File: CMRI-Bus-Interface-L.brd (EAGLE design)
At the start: 66 x 100 mm, 20 parts, among them CON1 0.100, CON2 0.100, U1 MAX3465CPD

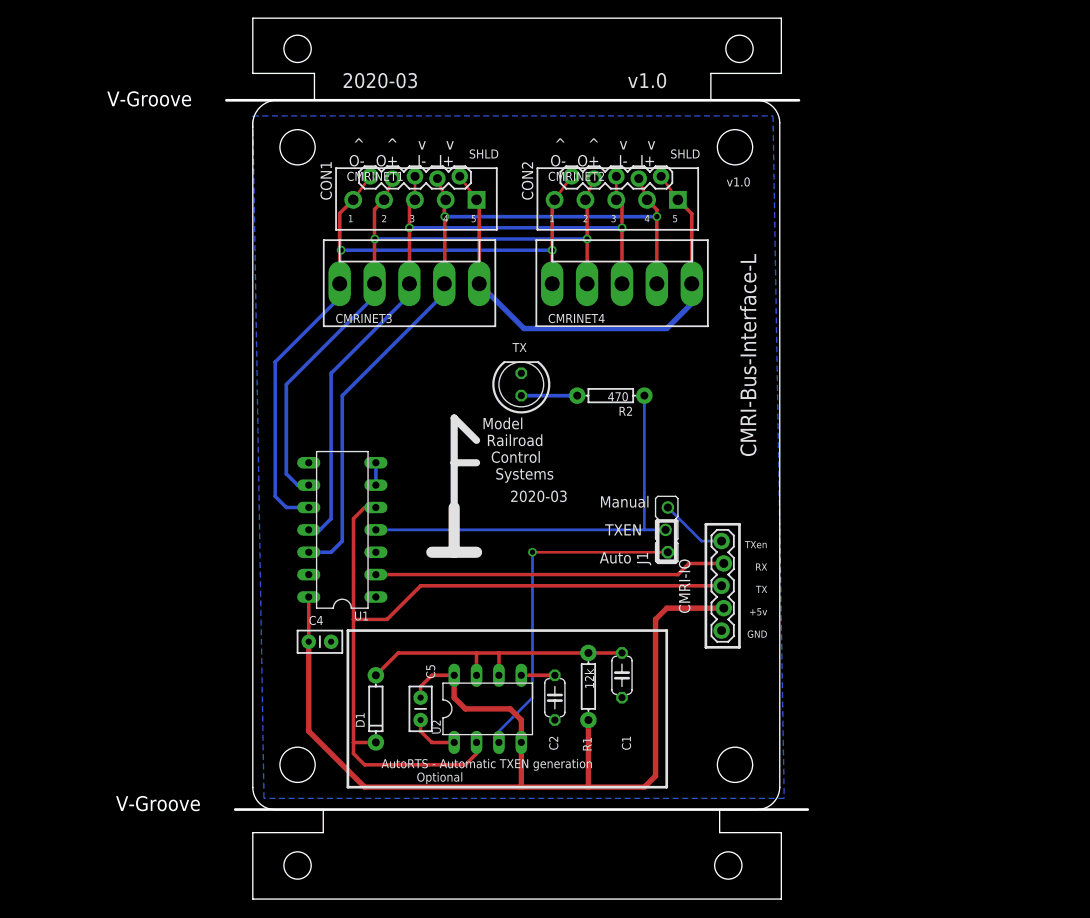
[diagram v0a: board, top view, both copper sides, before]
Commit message: v1.1 - changed BOARD to be a 10cmx10cm size so that V-Scores allowed
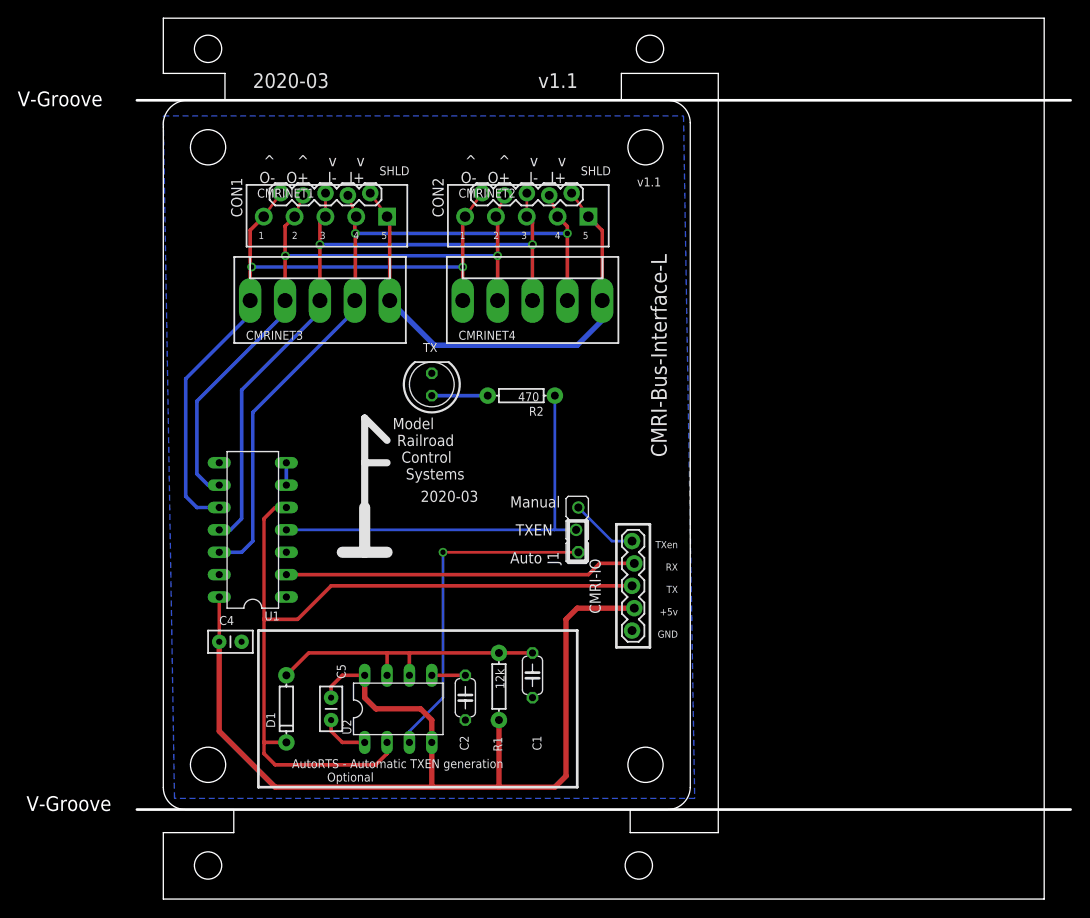
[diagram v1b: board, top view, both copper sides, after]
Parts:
- moved CMRINET4 10.3 mm to (41.9, 67.9)
- moved CMRINET1 10.3 mm to (17.8, 77.5)
- moved CMRINET3 10.3 mm to (17.8, 67.9)
- moved CON1 10.3 mm to (13.3, 80.0)
- moved CMRINET2 10.3 mm to (40.6, 77.5)
- moved CON2 10.3 mm to (36.2, 80.0)
- moved C1 10.2 mm to (41.9, 25.4)
- moved C2 10.2 mm to (34.3, 22.9)
- moved U$3 10.2 mm to (22.9, 39.4)
- moved BOARD1 10.2 mm to (0.00, 0.00)
- moved C4 10.2 mm to (7.62, 29.2)
- moved C5 10.2 mm to (19.1, 21.6)
- moved TX 10.2 mm to (30.5, 58.4)
- moved U1 10.2 mm to (10.2, 41.9)
- moved D1 10.2 mm to (14.0, 21.6)
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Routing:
- net OUT-: track 82.1 -> 80.2 mm
- net IN+: track 87.2 -> 85.3 mm
- net OUT+: track 77.9 -> 75.9 mm
- net IN-: track 82.5 -> 80.6 mm
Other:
- board size 66 x 100 mm -> 106 x 100 mm
- board text added: "v1.1"
- board text removed: "v1.0"

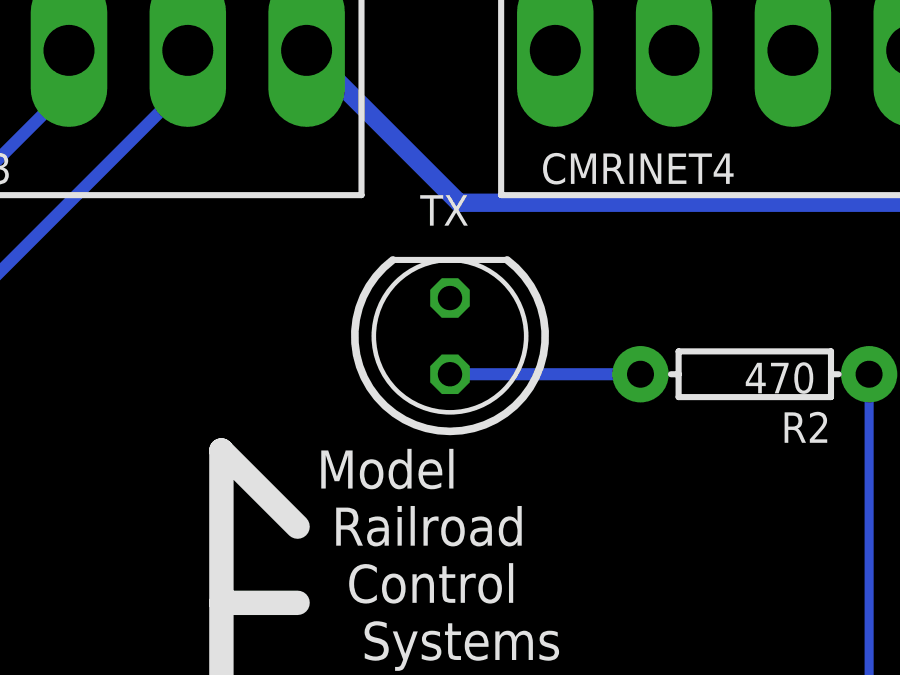
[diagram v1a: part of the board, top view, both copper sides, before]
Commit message: added missing component values
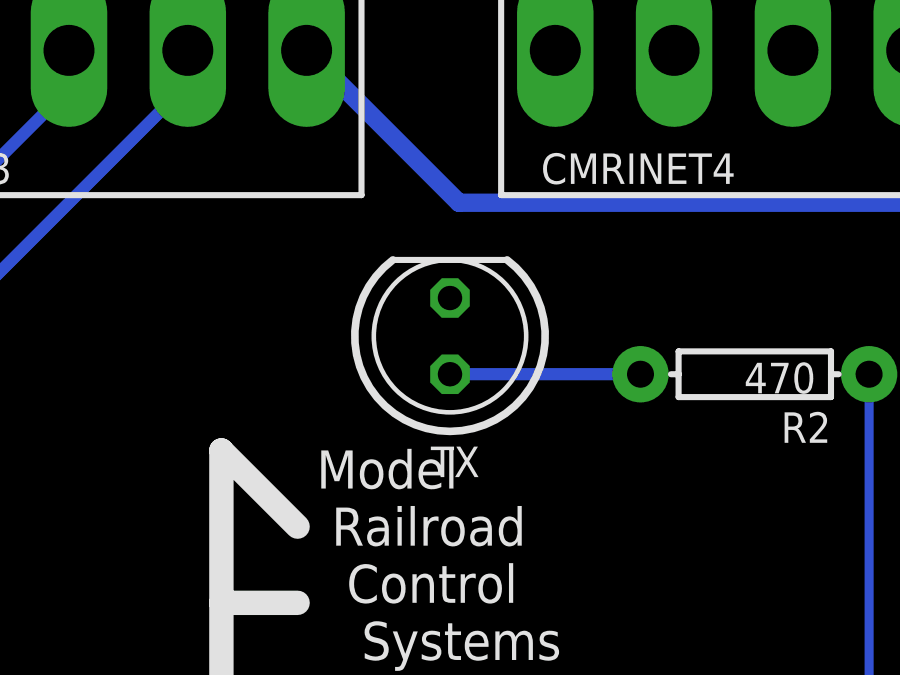
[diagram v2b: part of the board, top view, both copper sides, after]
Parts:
- CMRI-IO: value (none) -> 0.100; device SPCoast:CON-CMRI-IO -> SPCoast:1X05-CMRI-IO
- CMRINET3, CMRINET4: value Molex -> 0.156
- U2: value (none) -> NE555
- turned TX to 270 degrees
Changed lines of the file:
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@@
 <layer number="20" name="Dimension" color="15" fill="1" visible="yes" active="yes"/>
 <layer number="21" name="tPlace" color="19" fill="1" visible="yes" active="yes"/>
-<layer number="22" name="bPlace" color="17" fill="1" visible="yes" active="yes"/>
+<layer number="22" name="bPlace" color="17" fill="1" visible="no" active="yes"/>
 <layer number="23" name="tOrigins" color="30" fill="1" visible="yes" active="yes"/>
-<layer number="24" name="bOrigins" color="15" fill="1" visible="yes" active="yes"/>
+<layer number="24" name="bOrigins" color="15" fill="1" visible="no" active="yes"/>
 <layer number="25" name="tNames" color="63" fill="1" visible="yes" active="yes"/>
-<layer number="26" name="bNames" color="34" fill="1" visible="yes" active="yes"/>
+<layer number="26" name="bNames" color="34" fill="1" visible="no" active="yes"/>
 <layer number="27" name="tValues" color="56" fill="1" visible="yes" active="yes"/>
-<layer number="28" name="bValues" color="7" fill="1" visible="yes" active="yes"/>
-<layer number="29" name="tStop" color="7" fill="3" visible="yes" active="yes"/>
-<layer number="30" name="bStop" color="7" fill="6" visible="yes" active="yes"/>
-<layer number="31" name="tCream" color="7" fill="4" visible="yes" active="yes"/>
-<layer number="32" name="bCream" color="7" fill="5" visible="yes" active="yes"/>
-<layer number="33" name="tFinish" color="6" fill="3" visible="yes" active="yes"/>
-<layer number="34" name="bFinish" color="6" fill="6" visible="yes" active="yes"/>
-<layer number="35" name="tGlue" color="7" fill="4" visible="yes" active="yes"/>
-<layer number="36" name="bGlue" color="7" fill="5" visible="yes" active="yes"/>
-<layer number="37" name="tTest" color="7" fill="1" visible="yes" active="yes"/>
-<layer number="38" name="bTest" color="7" fill="1" visible="yes" active="yes"/>
-<layer number="39" name="tKeepout" color="4" fill="11" visible="yes" active="yes"/>
-<layer number="40" name="bKeepout" color="3" fill="11" visible="yes" active="yes"/>
-<layer number="41" name="tRestrict" color="4" fill="10" visible="yes" active="yes"/>
-<layer number="42" name="bRestrict" color="3" fill="10" visible="yes" active="yes"/>
-<layer number="43" name="vRestrict" color="2" fill="10" visible="yes" active="yes"/>
+<layer number="28" name="bValues" color="7" fill="1" visible="no" active="yes"/>
+<layer number="29" name="tStop" color="7" fill="3" visible="no" active="yes"/>
+<layer number="30" name="bStop" color="7" fill="6" visible="no" active="yes"/>
+<layer number="31" name="tCream" color="7" fill="4" visible="no" active="yes"/>
+<layer number="32" name="bCream" color="7" fill="5" visible="no" active="yes"/>
+<layer number="33" name="tFinish" color="6" fill="3" visible="no" active="yes"/>
+<layer number="34" name="bFinish" color="6" fill="6" visible="no" active="yes"/>
+<layer number="35" name="tGlue" color="7" fill="4" visible="no" active="yes"/>
+<layer number="36" name="bGlue" color="7" fill="5" visible="no" active="yes"/>
+<layer number="37" name="tTest" color="7" fill="1" visible="no" active="yes"/>
+<layer number="38" name="bTest" color="7" fill="1" visible="no" active="yes"/>
+<layer number="39" name="tKeepout" color="4" fill="11" visible="no" active="yes"/>
+<layer number="40" name="bKeepout" color="3" fill="11" visible="no" active="yes"/>
+<layer number="41" name="tRestrict" color="4" fill="10" visible="no" active="yes"/>
+<layer number="42" name="bRestrict" color="3" fill="10" visible="no" active="yes"/>
+<layer number="43" name="vRestrict" color="2" fill="10" visible="no" active="yes"/>
 <layer number="44" name="Drills" color="16" fill="1" visible="yes" active="yes"/>
 <layer number="45" name="Holes" color="35" fill="1" visible="yes" active="yes"/>
@@
 <layer number="48" name="Document" color="47" fill="1" visible="yes" active="yes"/>
 <layer number="49" name="Reference" color="48" fill="1" visible="yes" active="yes"/>
-<layer number="50" name="dxf" color="7" fill="1" visible="yes" active="yes"/>
+<layer number="50" name="dxf" color="7" fill="1" visible="no" active="yes"/>
 <layer number="51" name="tDocu" color="24" fill="1" visible="yes" active="yes"/>
-<layer number="52" name="bDocu" color="7" fill="1" visible="yes" active="yes"/>
+<layer number="52" name="bDocu" color="7" fill="1" visible="no" active="yes"/>
 <layer number="91" name="Nets" color="2" fill="1" visible="no" active="no"/>
 <layer number="92" name="Busses" color="1" fill="1" visible="no" active="no"/>
@@
 <attribute name="VALUE" x="42.672" y="57.531" size="1.016" layer="21" font="vector" ratio="15" rot="R180"/>
 </element>
-<element name="CMRINET3" library="SPCoast" package="KK-156-5" value="Molex" x="17.78" y="67.945" smashed="yes">
+<element name="CMRINET3" library="SPCoast" package="KK-156-5" value="0.156" x="17.78" y="67.945" smashed="yes">
 <attribute name="NAME" x="15.875" y="64.51" size="1.016" layer="25" font="vector" ratio="10" rot="R180"/>
 <attribute name="VALUE" x="25.4" y="65.03" size="1.016" layer="27" font="vector" ratio="10" rot="R180"/>
 </element>
-<element name="CMRINET4" library="SPCoast" package="KK-156-5" value="Molex" x="41.91" y="67.945" smashed="yes">
+<element name="CMRINET4" library="SPCoast" package="KK-156-5" value="0.156" x="41.91" y="67.945" smashed="yes">
 <attribute name="NAME" x="40.005" y="64.51" size="1.016" layer="25" font="vector" ratio="10" rot="R180"/>
 <attribute name="VALUE" x="50.165" y="65.03" size="1.016" layer="27" font="vector" ratio="10" rot="R180"/>
 </element>
-<element name="TX" library="SPCoast" package="LED5MM" value="" x="30.48" y="58.42" smashed="yes" rot="R90">
-<attribute name="NAME" x="31.115" y="63.119" size="1.016" layer="25" font="vector" ratio="10" rot="R180"/>
-<attribute name="VALUE" x="32.131" y="60.325" size="1.27" layer="27" ratio="10" rot="R90"/>
+<element name="TX" library="SPCoast" package="LED5MM" value="" x="30.48" y="58.42" smashed="yes" rot="R270">
+<attribute name="NAME" x="29.845" y="53.721" size="1.016" layer="25" font="vector" ratio="10"/>
+<attribute name="VALUE" x="28.829" y="56.515" size="1.27" layer="27" ratio="10" rot="R270"/>
 </element>
 <element name="U1" library="SPCoast" package="DIL14" value="MAX3465CPD" x="10.16" y="41.91" smashed="yes" rot="R90">
@@
 <attribute name="VALUE" x="10.795" y="35.179" size="1.016" layer="27" font="vector" ratio="10" rot="R90"/>
 </element>
-<element name="U2" library="SPCoast" package="DIL-08" value="" x="26.67" y="21.59" smashed="yes">
+<element name="U2" library="SPCoast" package="DIL-08" value="NE555" x="26.67" y="21.59" smashed="yes">
 <attribute name="MF" value="Arrow Electronics" x="26.67" y="21.59" size="1.778" layer="27" display="off"/>
 <attribute name="OC_NEWARK" value="89K1486" x="26.67" y="21.59" size="1.778" layer="27" display="off"/>
@@
 <attribute name="VALUE" x="31.75" y="76.2" size="1.016" layer="27" font="vector" ratio="10" rot="R180"/>
 </element>
-<element name="CMRI-IO" library="SPCoast" package="CON-CMRI-IO" value="" x="53.34" y="30.48" smashed="yes" rot="R90">
+<element name="CMRI-IO" library="SPCoast" package="1X05-CMRI-IO" value="0.100" x="53.34" y="30.48" smashed="yes" rot="R90">
 <attribute name="NAME" x="49.657" y="32.385" size="1.27" layer="25" font="vector" rot="R90"/>
 <attribute name="VALUE" x="56.642" y="29.21" size="1.27" layer="27" font="vector" rot="R90"/>

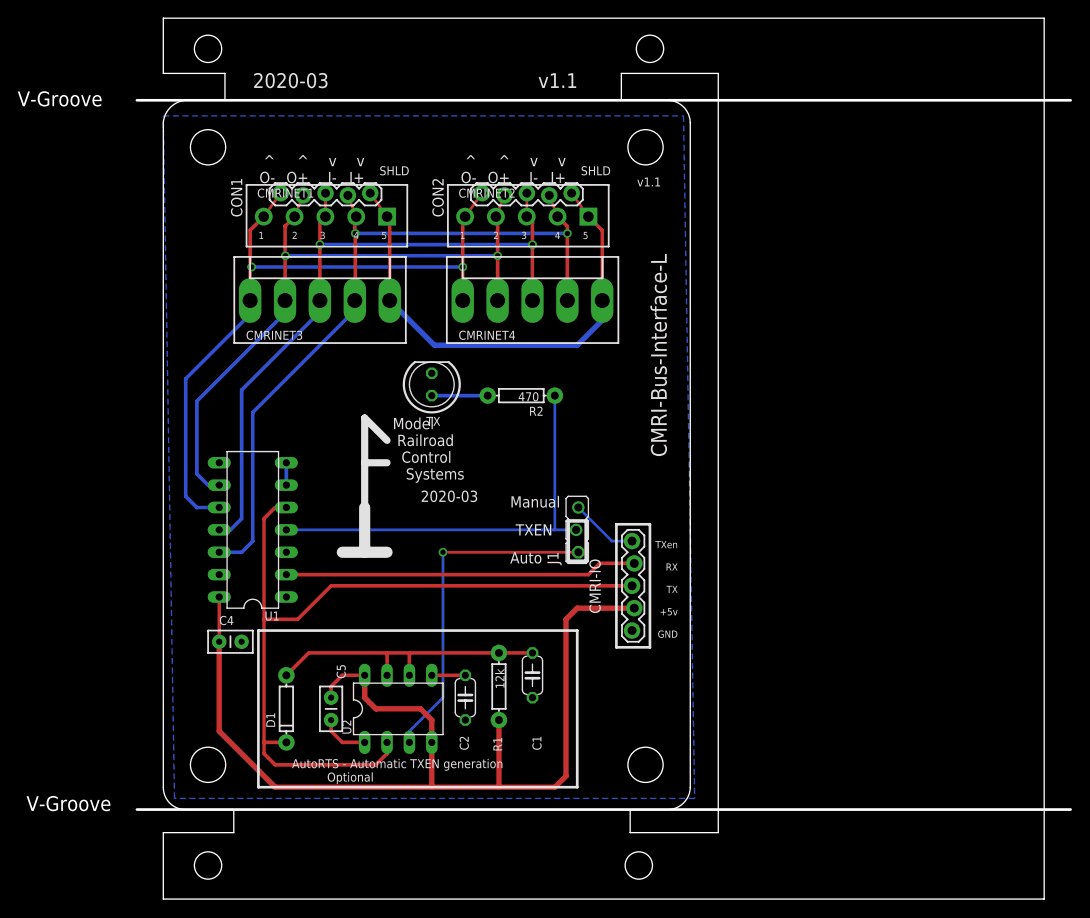
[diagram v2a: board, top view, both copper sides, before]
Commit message: SMT cost reduce
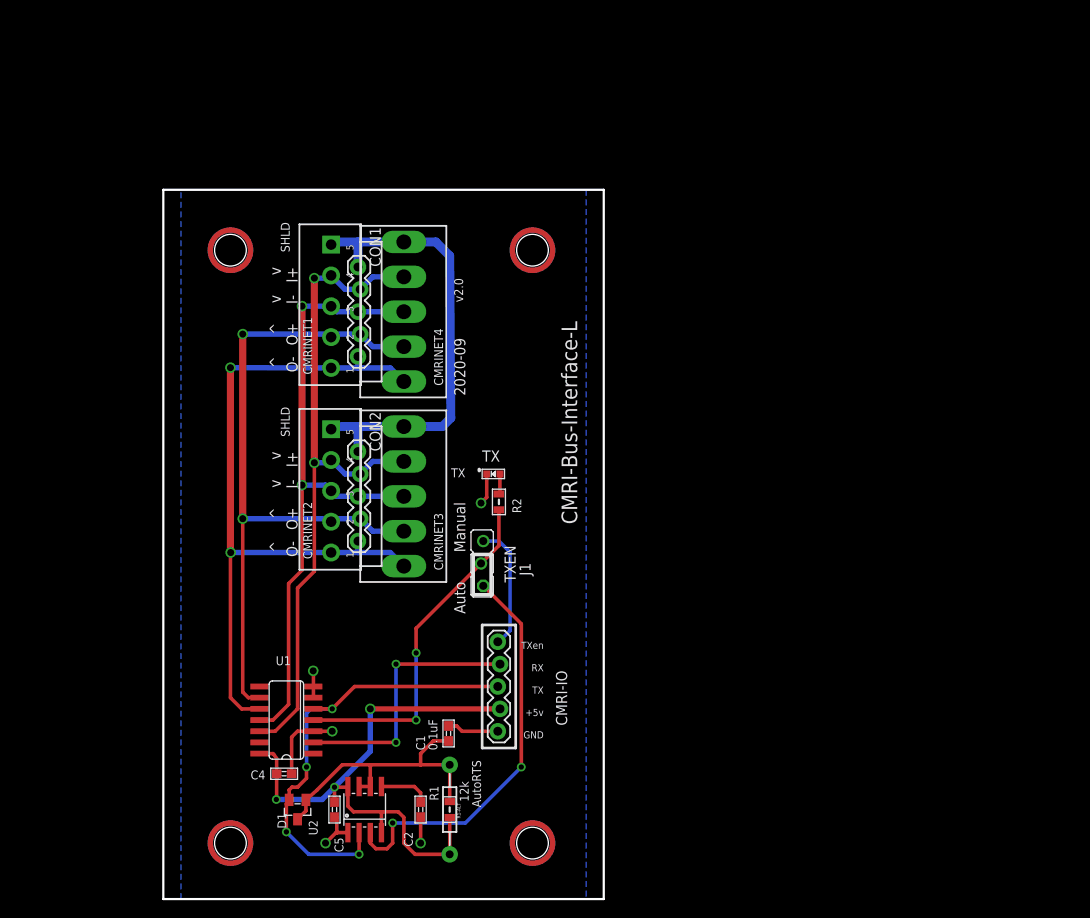
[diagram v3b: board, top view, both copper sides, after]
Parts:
- removed BOARD1: BOARD80X60, SPCoast:BOARD-DINRAIL-3.17INX6CM
- removed U$3: (no value), SPCoast:MRCS-LOGO
- added M1, M2, M3, M4: MOUNTINGHOLE, SPCoast:MOUNTINGHOLE
- added R1-ALT: 12k, SPCoast:0805-RES
- C1, C2: device SPCoast:C050-024X044 -> SPCoast:0603-CAP
- C4, C5: device SPCoast:C-PTH-0.100 -> SPCoast:0603-CAP
- D1: value 1N4148 -> BAV199; device SPCoast:DIODE-1N4148 -> SPCoast:SOT23
- R1: device SPCoast:AXIAL-0.3-RES -> SPCoast:AXIAL-0.4-RES
- R2: device SPCoast:AXIAL-0.3-RES -> SPCoast:0805-RES
- TX: value (none) -> Y; device SPCoast:LED5MM -> SPCoast:0603-LED
- U1: value MAX3465CPD -> MAX3465CSD; device SPCoast:DIL14 -> SPCoast:SO14
- U2: device SPCoast:DIL-08 -> SPCoast:SO08
- moved CON2 41.8 mm to (22.2, 40.6), turned to 90 degrees
- moved CMRINET2 38.4 mm to (19.1, 45.7), turned to 90 degrees
- moved CMRINET3 24.2 mm to (27.3, 45.7), turned to 90 degrees
- moved U1 21.9 mm to (14.0, 20.3)
- moved CON1 20.4 mm to (22.2, 61.6), turned to 90 degrees
- moved CMRI-IO 19.1 mm to (38.1, 19.1)
- moved C4 16.2 mm to (13.7, 14.2)
- moved R1 15.0 mm to (32.5, 10.2)
- moved CMRINET4 14.7 mm to (27.3, 66.7), turned to 90 degrees
- moved C2 13.7 mm to (29.2, 10.2)
- moved TX 12.3 mm to (37.5, 48.3), turned to 0 degrees
- moved R2 12.3 mm to (38.1, 45.1), turned to 90 degrees
- moved U2 12.0 mm to (22.9, 10.2)
- moved C1 11.6 mm to (32.4, 18.8), turned to 90 degrees
- moved D1 11.5 mm to (15.2, 10.2)
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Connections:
- net GND: now also TX.C; no longer TX.K
- net N$29: now also R2.2; no longer R2.P$2
- net N$52: now also D1.1, D1.3, R1-ALT.1; no longer D1.A
- net TX: now also D1.2; no longer D1.C
- net TXEN: now also R2.1; no longer R2.P$1
- net VCC: now also R1-ALT.2
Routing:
- net VCC: track 115.9 -> 67.7 mm, vias 0 -> 3
- net TX: track 90.7 -> 51.7 mm, vias 0 -> 4
- net GND: track 8.15 -> 29.6 mm, vias 0 -> 5
- net RX: track 40.0 -> 30.1 mm, vias 0 -> 2
- net TXEN: track 48.1 -> 39.4 mm, vias 0 -> 2
- net TXEN-AUTO: track 38.5 -> 46.1 mm, vias 1 -> 2
- net IN+: track 85.3 -> 78.1 mm
- net IN-: track 80.6 -> 73.8 mm
- net TXEN-MANUAL: track 7.67 -> 14.4 mm
- net OUT+: track 75.9 -> 81.1 mm
- net OUT-: track 80.2 -> 84.5 mm
- net N$29: track 6.35 -> 2.32 mm
- net SHIELD: track 56.0 -> 52.6 mm
- net N$38: track 3.81 -> 5.79 mm
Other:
- board size 106 x 100 mm -> 50 x 80.5 mm
- board text added: "2020-09"
- board text added: "AutoRTS"
- board text added: "C1"
- board text added: "C2"
- board text added: "C4"
- board text added: "C5"
- board text added: "CMRI-IO"
- board text added: "CMRINET1"
- board text added: "CMRINET2"
- board text added: "CMRINET3"
- board text added: "CMRINET4"
- board text added: "CON1"
- board text added: "CON2"
- board text added: "D1"
- board text added: "J1"
- board text added: "MRCS Design Chuck Catania John Plocher"
- board text added: "R1"
- board text added: "R1-ALT"
- board text added: "R2"
- board text added: "TX"
- board text added: "U1"
- board text added: "U2"
- board text added: "v2.0"
- board text removed: "115200 1000 0.1 uF"
- board text removed: "19200 12000 0.1 uF"
- board text removed: "2020-03"
- board text removed: "28800 3300 0.1 uF"
- board text removed: "38400 3000 0.1 uF"
- board text removed: "57600 2000 0.1 uF"
- board text removed: "9600 12000 0.1 uF"
- board text removed: "AutoRTS - Automatic TXEN generation Optional"
- board text removed: "AutoRTS Values"
- board text removed: "BPS R1 C1"
- board text removed: "v1.1"
